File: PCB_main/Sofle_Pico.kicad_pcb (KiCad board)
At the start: 2 copper layers, 162.5 x 106 mm, 68 parts, among them J1 Conn_02x08_Top_Bottom, J2 Conn_02x08_Top_Bottom, J3 Conn_01x06, SW1 SW_PUSH, SW10 SW_PUSH, SW11 SW_PUSH, SW12 SW_PUSH, SW13 SW_PUSH, SW14 SW_PUSH, SW15 SW_PUSH, SW16 SW_PUSH, SW17 SW_PUSH, SW18 SW_PUSH, SW2 SW_PUSH, SW20 SW_PUSH, SW21 SW_PUSH, SW22 SW_PUSH, SW23 SW_PUSH, SW24 SW_PUSH, SW27 SW_PUSH, SW28 SW_PUSH, SW29 SW_PUSH, SW3 SW_PUSH, SW30 SW_PUSH, SW37 SW_PUSH, SW38 SW_PUSH, SW39 SW_PUSH, SW4 SW_PUSH, SW40 SW_PUSH, SW41 SW_PUSH, SW5 SW_PUSH, SW6 SW_PUSH, SW7 SW_PUSH, SW8 SW_PUSH, SW9 SW_PUSH, U2 Pico

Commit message: improve positioning
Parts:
- J3: value Conn_01x06 -> Conn_02x03; footprint Connector_PinHeader_1.27mm:PinHeader_1x06_P1.27mm_Horizontal -> Connector_PinHeader_2.54mm:PinHeader_2x03_P2.54mm_Vertical
- U2: footprint Module:RaspberryPi_Pico_SMD_HandSolder -> Module:RaspberryPi_Pico_SMD
- moved D11 7.40 mm to (196.7, 73.7)
- moved D17 7.40 mm to (196.7, 92.7)
- moved D23 7.40 mm to (196.8, 111.6)
- moved SW11 7.40 mm to (196.8, 64.0)
- moved SW17 7.40 mm to (196.8, 83.1)
- moved D5 7.40 mm to (196.7, 54.6)
- moved SW5 7.40 mm to (196.8, 45.0)
- moved SW23 7.40 mm to (196.8, 102.2)
- moved SW29 7.40 mm to (196.8, 121.2)
- moved J3 7.25 mm to (128.0, 105.5), turned to 45 degrees
- moved D29 5.54 mm to (196.4, 130.5)
- moved D10 5.00 mm to (177.7, 71.2)
- moved D16 5.00 mm to (177.7, 90.2)
- moved D22 5.00 mm to (177.7, 109.3)
- moved D28 5.00 mm to (177.7, 128.0)
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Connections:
- J3 pad 1: row5 -> lcol0
- J3 pad 2: lcol0 -> lcol1
- J3 pad 3: lcol1 -> lcol2
- J3 pad 4: lcol2 -> lcol3
- J3 pad 5: lcol3 -> unconnected-(J3-Pin_5-Pad5)
- J3 pad 6: unconnected-(J3-Pin_6-Pad6) -> row5
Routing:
- net Net-(D29-A): track 0.00 -> 6.64 mm
- net Net-(D23-A): track 6.64 -> 0.00 mm
- net GND: track 29.7 -> 23.7 mm
- net lcol4: track 0.00 -> 4.50 mm
- net lcol5: track 0.00 -> 1.50 mm
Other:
- board size 162.5 x 106 mm -> 162.5 x 103 mm

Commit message: more pcb progress
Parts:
- J1, J2: footprint Connector_PinHeader_1.27mm:PinHeader_2x08_P1.27mm_Horizontal -> Connector_PinHeader_2.00mm:PinHeader_2x08_P2.00mm_Vertical
- moved J1 46.9 mm to (124.5, 38.0), turned to 90 degrees
- moved J2 33.0 mm to (90.3, 38.0), turned to 90 degrees
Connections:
- J1 pad 1: rcol0 -> rcol6
- J1 pad 10: row1 -> unconnected-(J1-Pin_10-Pad10)
- J1 pad 11: row3 -> row5
- J1 pad 12: row3 -> row4
- J1 pad 13: row4 -> row3
- J1 pad 14: row5 -> row2
- J1 pad 15: unconnected-(J1-Pin_15-Pad15) -> row1
- J1 pad 16: unconnected-(J1-Pin_16-Pad16) -> row0
- J1 pad 2: rcol1 -> rcol5
- J1 pad 3: rcol2 -> rcol4
- J1 pad 5: rcol4 -> rcol2
- J1 pad 6: rcol5 -> rcol1
- J1 pad 7: rcol6 -> rcol0
- J1 pad 9: row0 -> unconnected-(J1-Pin_9-Pad9)
- J2 pad 1: lcol0 -> lcol6
- J2 pad 10: row1 -> unconnected-(J2-Pin_10-Pad10)
- J2 pad 11: row3 -> row5
- J2 pad 12: row3 -> row4
- J2 pad 13: row4 -> row3
- J2 pad 14: row5 -> row2
- J2 pad 15: unconnected-(J2-Pin_15-Pad15) -> row1
- J2 pad 16: unconnected-(J2-Pin_16-Pad16) -> row0
- J2 pad 2: lcol1 -> lcol5
- J2 pad 3: lcol2 -> lcol4
- J2 pad 5: lcol4 -> lcol2
- J2 pad 6: lcol5 -> lcol1
- J2 pad 7: lcol6 -> lcol0
- J2 pad 9: row0 -> unconnected-(J2-Pin_9-Pad9)
- U2 pad 1: lcol0 -> row0
- U2 pad 10: unconnected-(U2-GPIO7-Pad10) -> rcol6
- U2 pad 14: row0 -> rcol5
- U2 pad 15: row1 -> rcol4
- U2 pad 16: row2 -> rcol3
- U2 pad 17: row3 -> rcol2
- U2 pad 19: row4 -> rcol1
- U2 pad 2: lcol1 -> row1
- U2 pad 20: row5 -> rcol0
- U2 pad 21: unconnected-(U2-GPIO16-Pad21) -> lcol0
- U2 pad 22: unconnected-(U2-GPIO17-Pad22) -> lcol1
- U2 pad 24: unconnected-(U2-GPIO18-Pad24) -> lcol2
- U2 pad 25: rcol6 -> lcol3
- U2 pad 26: rcol5 -> lcol4
- U2 pad 27: rcol4 -> lcol5
- U2 pad 29: rcol3 -> lcol6
- U2 pad 31: rcol2 -> unconnected-(U2-GPIO26_ADC0-Pad31)
- U2 pad 32: rcol1 -> unconnected-(U2-GPIO27_ADC1-Pad32)
- U2 pad 34: rcol0 -> unconnected-(U2-GPIO28_ADC2-Pad34)
- U2 pad 4: lcol2 -> row2
- U2 pad 5: lcol3 -> row3
- U2 pad 6: lcol4 -> row4
- U2 pad 7: lcol5 -> row5
- U2 pad 9: lcol6 -> unconnected-(U2-GPIO6-Pad9)
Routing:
- net lcol6: track 0.00 -> 306.7 mm, vias 0 -> 1
- net lcol5: track 1.50 -> 290.0 mm, vias 0 -> 1
- net lcol4: track 4.50 -> 272.9 mm, vias 0 -> 1
- net lcol3: track 0.00 -> 250.5 mm, vias 0 -> 1
- net lcol2: track 0.00 -> 228.6 mm, vias 0 -> 1
- net lcol1: track 0.00 -> 198.4 mm, vias 0 -> 1
- net lcol0: track 0.00 -> 171.2 mm, vias 0 -> 1
- net row4: track 0.00 -> 157.4 mm, vias 0 -> 2
- net row3: track 0.00 -> 119.6 mm, vias 0 -> 1
- net row2: track 0.00 -> 93.5 mm, vias 0 -> 1
- net row1: track 0.00 -> 74.7 mm, vias 0 -> 3
- net rcol1: track 0.00 -> 57.7 mm, vias 0 -> 1
- net rcol0: track 0.00 -> 56.4 mm, vias 0 -> 1
- net rcol3: track 0.00 -> 50.1 mm, vias 0 -> 1
- net rcol2: track 0.00 -> 50.0 mm, vias 0 -> 1
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
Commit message: more
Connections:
- J3 pad 5: unconnected-(J3-Pin_5-Pad5) -> lcol4
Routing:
- net row0: track 38.8 -> 166.3 mm
- net row1: track 74.7 -> 197.7 mm
- net row2: track 93.5 -> 211.7 mm
- net row3: track 119.6 -> 214.7 mm
- net row5: track 30.9 -> 114.8 mm, vias 0 -> 1
- net row4: track 157.4 -> 233.4 mm
- net lcol4: track 272.9 -> 336.5 mm, vias 1 -> 2
- net lcol3: track 250.5 -> 296.9 mm, vias 1 -> 2
- net lcol2: track 228.6 -> 255.2 mm, vias 1 -> 2
- net Net-(D20-A): track 0.00 -> 6.02 mm
- net Net-(D13-A): track 0.00 -> 5.46 mm
- net Net-(D40-A): track 0.00 -> 5.30 mm
- net Net-(D31-A): track 0.00 -> 5.30 mm
- net Net-(D39-A): track 0.00 -> 5.30 mm
- net Net-(D38-A): track 0.00 -> 5.30 mm
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- added copper zone on F.Cu, net GND
- removed copper zone on F.Cu, net VSYS
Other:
- board text removed: "USB"

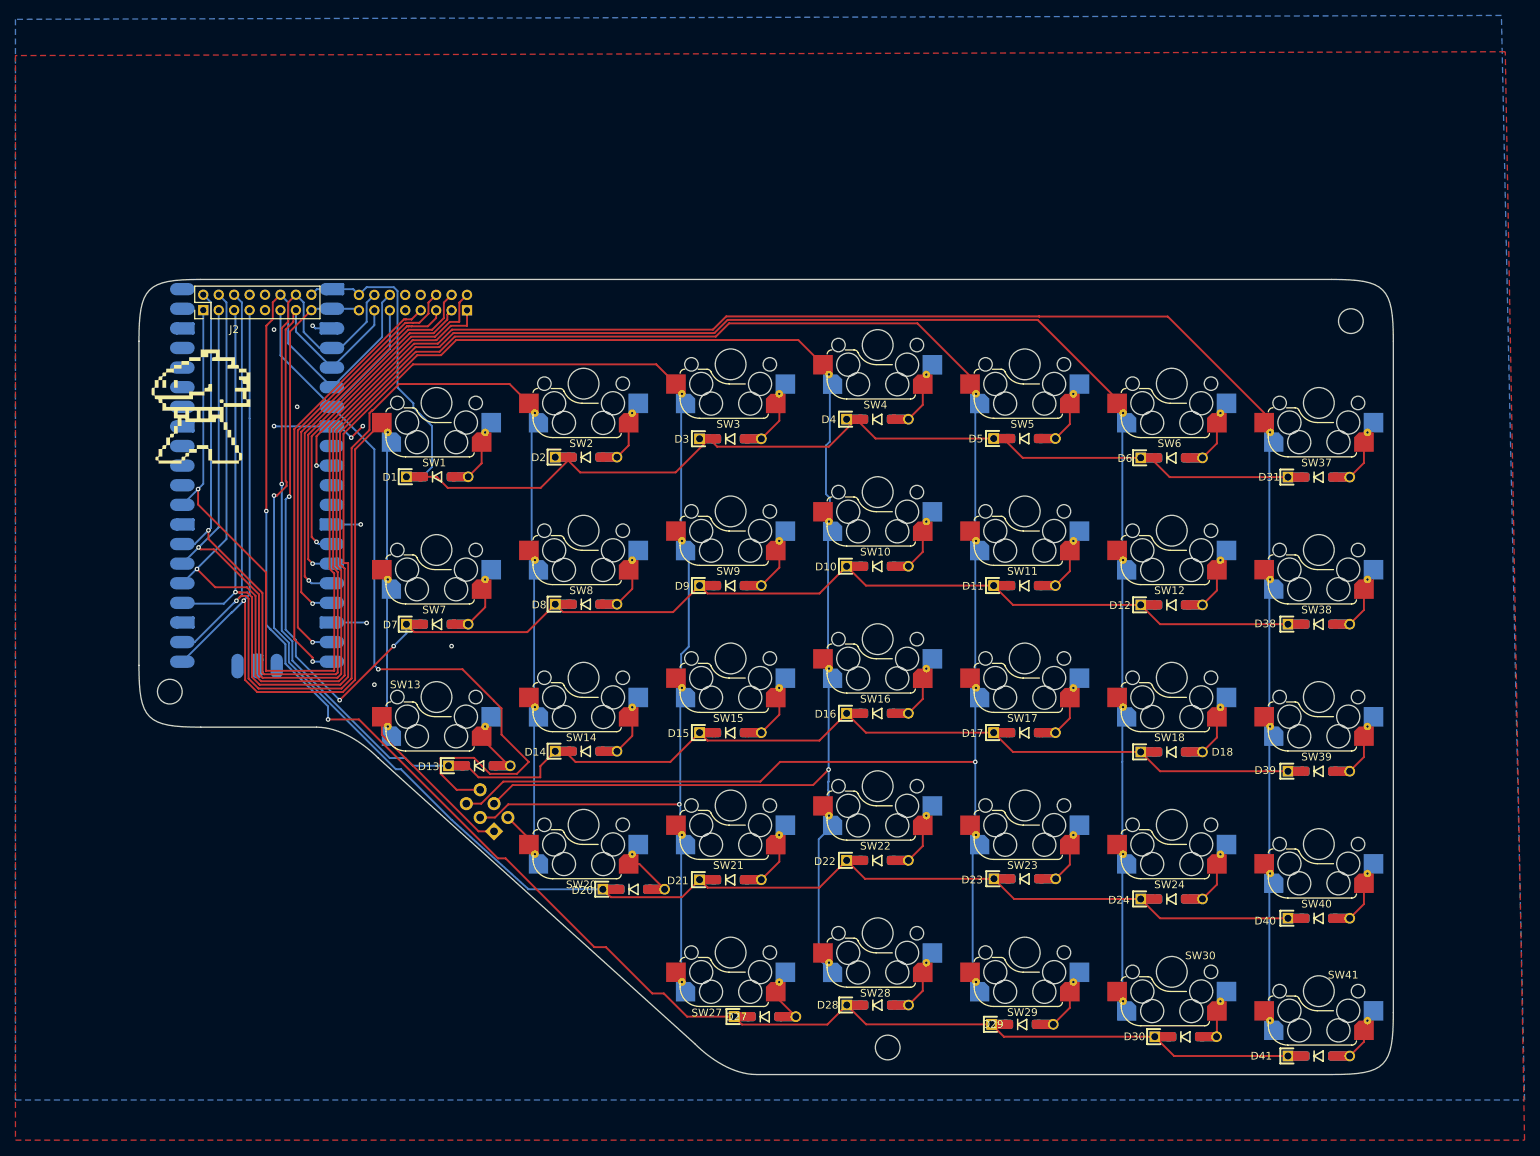
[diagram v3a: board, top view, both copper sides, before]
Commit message: rotate idc socket
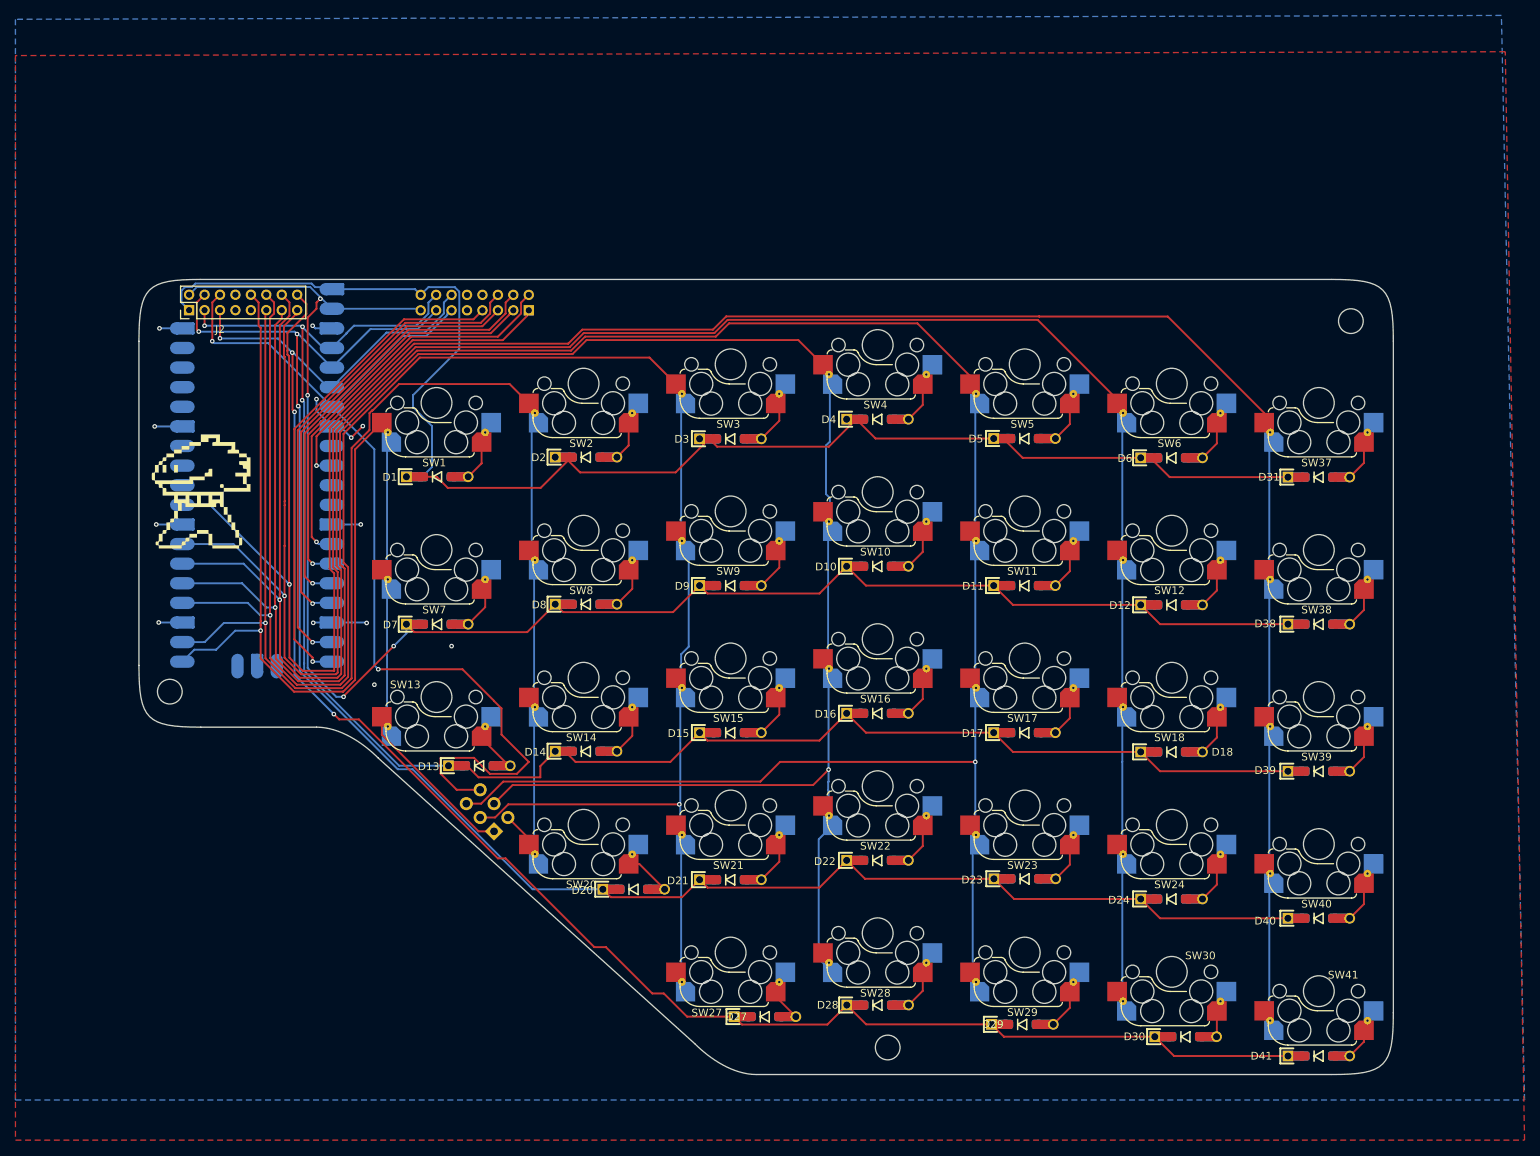
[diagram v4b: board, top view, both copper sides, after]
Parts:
- moved J1 8.00 mm to (132.5, 38.0)
- moved J2 1.84 mm to (88.5, 38.0)
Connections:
- J2 pad 1: lcol6 -> row0
- J2 pad 10: unconnected-(J2-Pin_10-Pad10) -> lcol0
- J2 pad 11: row5 -> lcol1
- J2 pad 12: row4 -> lcol2
- J2 pad 13: row3 -> lcol3
- J2 pad 14: row2 -> lcol4
- J2 pad 15: row1 -> lcol5
- J2 pad 16: row0 -> lcol6
- J2 pad 2: lcol5 -> row1
- J2 pad 3: lcol4 -> row2
- J2 pad 4: lcol3 -> row3
- J2 pad 5: lcol2 -> row4
- J2 pad 6: lcol1 -> row5
- J2 pad 7: lcol0 -> unconnected-(J2-Pin_7-Pad7)
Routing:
- net row0: track 166.3 -> 196.1 mm
- net row1: track 197.7 -> 222.1 mm, vias 3 -> 4
- net row3: track 214.7 -> 231.1 mm, vias 1 -> 3
- net row5: track 114.8 -> 130.4 mm, vias 1 -> 2
- net row2: track 211.7 -> 224.0 mm, vias 1 -> 3
- net GND: track 23.6 -> 35.9 mm, vias 10 -> 13
- net lcol6: track 305.6 -> 316.6 mm
- net rcol0: track 56.4 -> 64.4 mm
- net rcol1: track 56.8 -> 64.8 mm
- net rcol4: track 45.1 -> 52.7 mm
- net rcol3: track 50.1 -> 57.7 mm
- net rcol2: track 50.0 -> 57.4 mm
- net rcol5: track 45.3 -> 52.6 mm
- net rcol6: track 33.2 -> 40.4 mm
- net lcol1: track 198.4 -> 192.3 mm
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
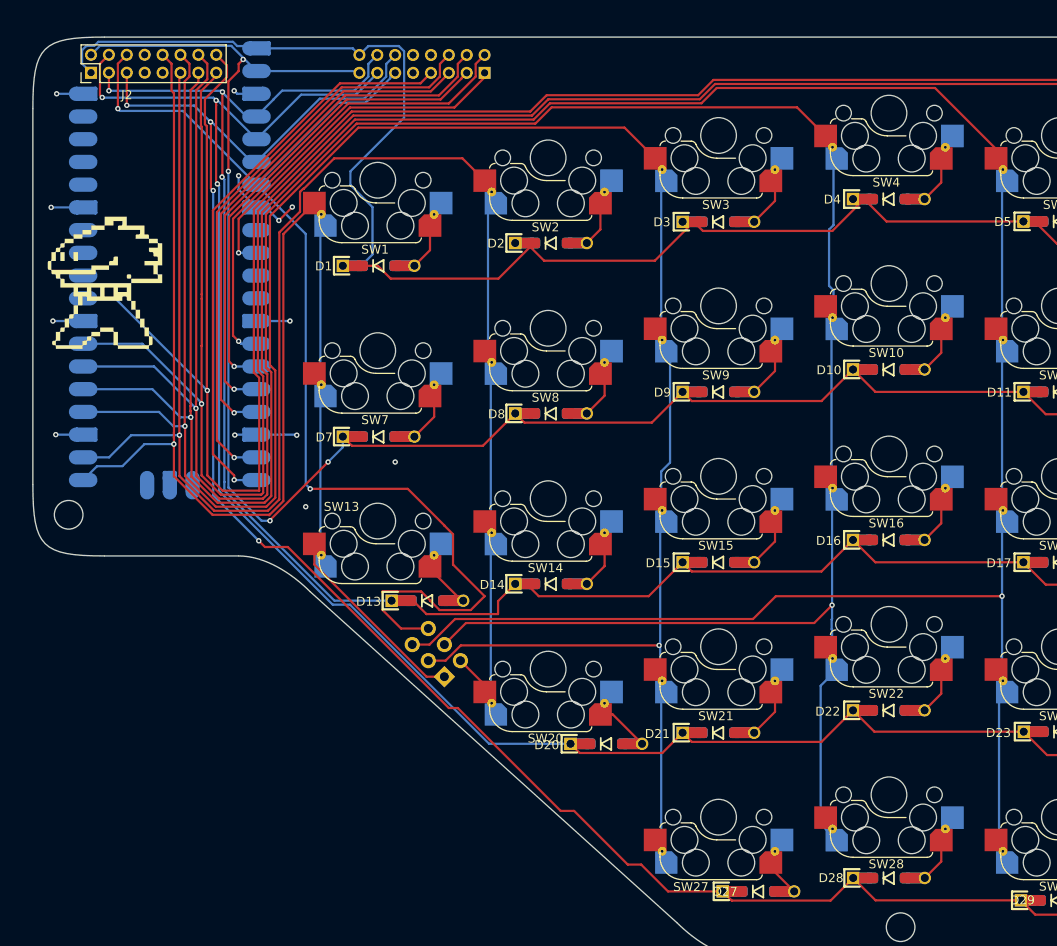
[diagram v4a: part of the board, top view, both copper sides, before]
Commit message: adjust holes
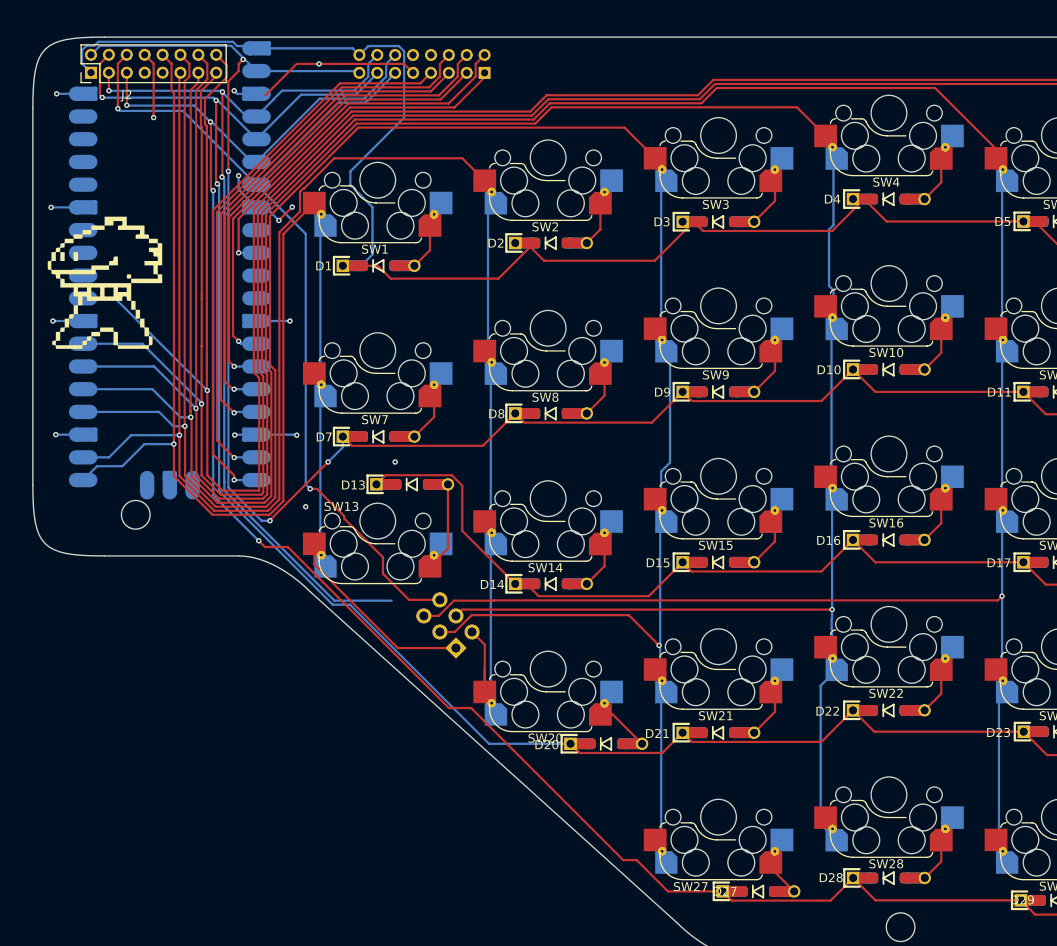
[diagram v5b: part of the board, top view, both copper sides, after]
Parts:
- moved D13 13.1 mm to (124.4, 84.0)
- moved J3 3.46 mm to (129.3, 102.3)
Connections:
- J1 pad 9: unconnected-(J1-Pin_9-Pad9) -> GND
- J2 pad 8: unconnected-(J2-Pin_8-Pad8) -> GND
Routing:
- net row5: track 130.4 -> 103.8 mm
- net GND: track 35.9 -> 61.7 mm, vias 13 -> 15
- net row2: track 224.0 -> 231.3 mm
- net lcol1: track 192.3 -> 197.6 mm
- net Net-(D13-A): track 5.46 -> 10.0 mm
- net lcol3: track 294.5 -> 291.7 mm
- net lcol4: track 341.8 -> 339.2 mm
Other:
- outline, holes or cut-outs redrawn
